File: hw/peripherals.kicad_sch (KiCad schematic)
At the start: 22 parts, among them Q2 N-Channel, SW1 SW_DPST, U10 MB85RC256VPNF-G-JNERE1, U11 DS3231M, U9 PCA9536D

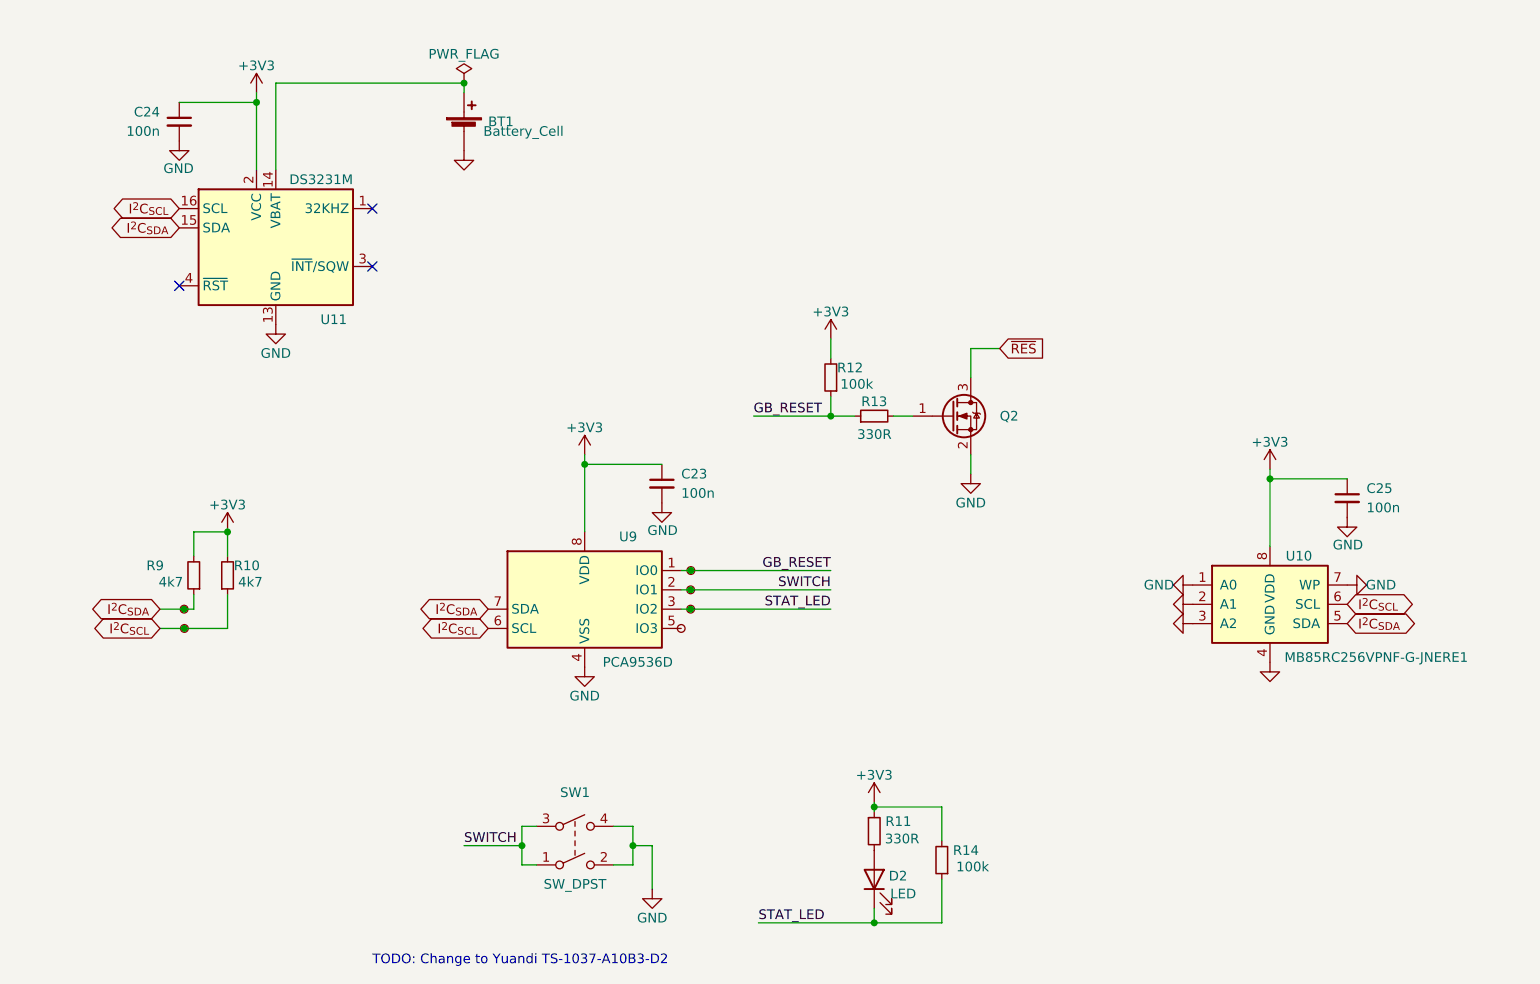
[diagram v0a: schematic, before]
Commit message: hw: multiplex Game Boy bus pins
Signed-off-by: Mahyar Koshkouei <mk@deltabeard.com>
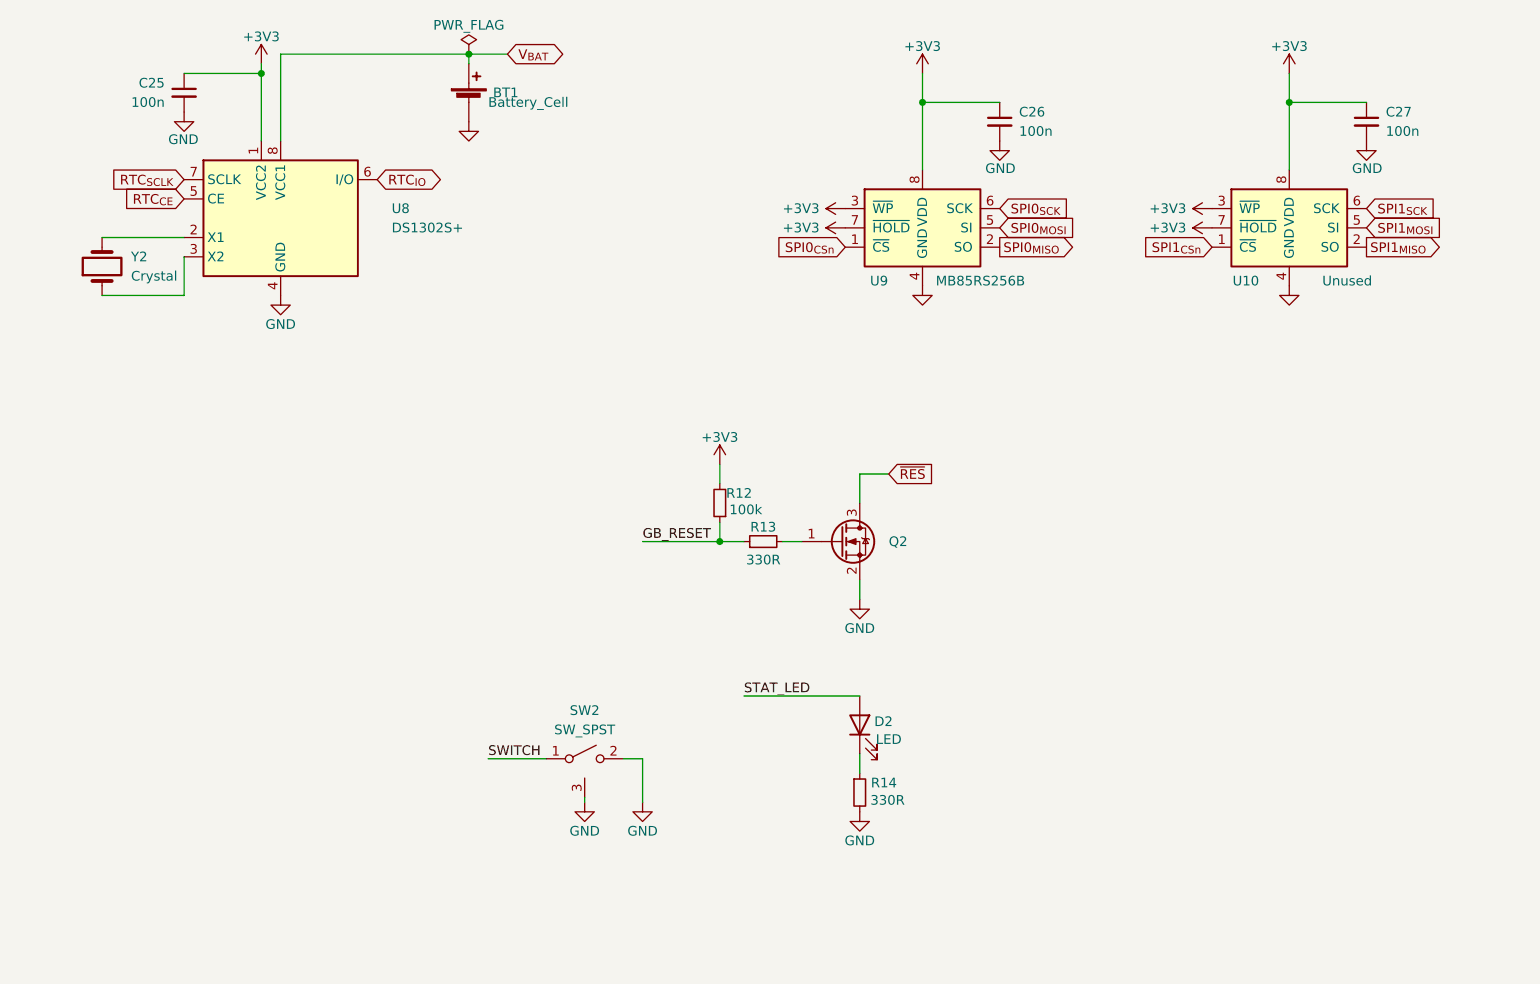
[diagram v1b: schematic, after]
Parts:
- removed C23: 100n, Capacitor_SMD:C_0402_1005Metric, symbol Device:C_Small
- removed R10, R9: 4k7, Resistor_SMD:R_0402_1005Metric, symbol Device:R_Small
- removed R14: 100k, Resistor_SMD:R_0603_1608Metric, symbol Device:R_Small
- removed SW1: SW_DPST, Project_Specific:K2-1114SA-A4SW-06, symbol Switch:SW_DPST
- removed TP40, TP41, TP42, TP43, TP44, TP45: TestPoint_Small, TestPoint:TestPoint_Pad_D1.0mm, symbol Connector:TestPoint_Small
- removed U10: MB85RC256VPNF-G-JNERE1, Package_SO:SOIC-8_3.9x4.9mm_P1.27mm, symbol Project_specific:MB85RC256V
- removed U11: DS3231M, Package_SO:SOIC-16W_7.5x10.3mm_P1.27mm, symbol Timer_RTC:DS3231M
- removed U9: PCA9536D, Package_SO:SOIC-8_3.9x4.9mm_P1.27mm, symbol Interface_Expansion:PCA9536D
- added C27: 100n, Capacitor_SMD:C_0402_1005Metric, symbol Device:C_Small
- added SW2: SW_SPST, symbol Switch:SW_SPST
- added U10: Unused, symbol Memory_NVRAM:MB85RS256B
- added U8: DS1302S+, Package_SO:SO-8_5.3x6.2mm_P1.27mm, symbol Timer_RTC:DS1302S+
- added U9: MB85RS256B, symbol Memory_NVRAM:MB85RS256B
- added Y2: Crystal, symbol Device:Crystal
- renumbered C24 to C25, C25 to C26, R11 to R14
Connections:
- net +3V3: now also C27.1, U10.3 (~{WP}), U10.7 (~{HOLD}), U10.8 (VDD), U8.1 (VCC2), U9.3 (~{WP}), U9.7 (~{HOLD}), U9.8 (VDD); no longer R14.1
- net GND: now also R14.2, C27.2, SW2.2 (B), SW2.3 (Shell), U10.4 (GND), U8.4 (GND), U9.4 (GND)
- net STAT_LED: now also D2.2 (A); no longer D2.1 (K)
- net SWITCH: now also SW2.1 (A)
- net V_{BAT}: now reaches BT1.1 (+)
- net V_{BAT}: now also U8.8 (VCC1)
- new net: D2.1 (K), R14.1
- new net: U8.2 (X1), Y2.2
- new net: U8.3 (X2), Y2.1
- new net RTC_{CE}: U8.5 (CE)
- new net RTC_{IO}: U8.6 (I/O)
- new net RTC_{SCLK}: U8.7 (SCLK)
- new net SPI0_{CSn}: U9.1 (~{CS})
- new net SPI0_{MISO}: U9.2 (SO)
- new net SPI0_{MOSI}: U9.5 (SI)
- new net SPI0_{SCK}: U9.6 (SCK)
- new net SPI1_{CSn}: U10.1 (~{CS})
- new net SPI1_{MISO}: U10.2 (SO)
- new net SPI1_{MOSI}: U10.5 (SI)
- new net SPI1_{SCK}: U10.6 (SCK)
- no-connect marks 3 -> 0
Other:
- note removed: "TODO: Change to Yuandi TS-1037-A10B3-D2"
- moved on the sheet: BT1, C25, C26, D2, Q2, R12, R13, R14

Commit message: hw: begin layout
Signed-off-by: Mahyar Koshkouei <mk@deltabeard.com>
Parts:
- removed C27: 100n, Capacitor_SMD:C_0402_1005Metric, symbol Device:C_Small
- removed U10: Unused, symbol Memory_NVRAM:MB85RS256B
- removed U8: DS1302S+, Package_SO:SO-8_5.3x6.2mm_P1.27mm, symbol Timer_RTC:DS1302S+
- removed Y2: Crystal, symbol Device:Crystal
- added U8: DS1307Z+, Package_SO:SO-8_3.9x4.9mm_P1.27mm, symbol Timer_RTC:DS1307Z+
- added Y2: 32.768k-12.5pF, Project_Specific:Crystal_DS26_D2.0mm_L6.0mm_Horizontal_1EP_style1, symbol Device:Crystal_Small
- SW3: renamed from SW2; footprint (none) -> Project_Specific:TS-1037-A10B3-D2; LCSC (none) -> C499330; MFr (none) -> TS-1037-A10B3-D2; Notes (none) -> Alternative manufacturer is acceptable
- U9: footprint (none) -> Package_SO:SOIC-8_3.9x4.9mm_P1.27mm; LCSC (none) -> C8742; MFr (none) -> MB85RS256BPNF-G-JNERE1; Manufacturer (none) -> Fujitsu; Notes (none) -> Alternative: FM25W256-GTR
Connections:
- net +3V3: now also U8.8 (VCC)
- net GND: now also U8.4 (GND)
- net V_{BAT}: now also U8.3 (VBAT)
- new net: U8.2 (X2), Y2.1
- new net: U8.1 (X1), Y2.2
- new net I2C_{SCLK}: U8.6 (SCL)
- new net I2C_{SDA}: U8.5 (SDA)
- no-connect marks 0 -> 1
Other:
- moved on the sheet: BT1, C25

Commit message: hw: WIP
Signed-off-by: Mahyar Koshkouei <mk@deltabeard.com>
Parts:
- removed SW3: SW_SPST, Project_Specific:TS-1037-A10B3-D2, symbol Switch:SW_SPST
- added C27: 100n, Capacitor_SMD:C_0402_1005Metric, symbol Device:C_Small
- added D3: SM4007PL, Diode_SMD:D_SOD-123F, symbol Diode:1N4448W
- added M1: Motor_DC, Connector_PinHeader_1.27mm:PinHeader_1x02_P1.27mm_Vertical, symbol Motor:Motor_DC
- added Q3: N-Channel, Package_TO_SOT_SMD:SOT-23, symbol Device:Q_NMOS_GSD
- added R14: 330R, Resistor_SMD:R_0603_1608Metric, symbol Device:R_Small
- added SW2: SW_SPST, Button_Switch_SMD:SW_SPST_TL3342, symbol Switch:SW_SPST
- Q2: Manufacturer Changjiang Electronics Tech (CJ) -> Changjiang Electronics Tech (CJ)
- R11: renamed from R12; Manufacturer UNI-ROYAL(Uniroyal Elec) -> UNI-ROYAL(Uniroyal Elec)
- R12: renamed from R13; Manufacturer UNI-ROYAL(Uniroyal Elec) -> UNI-ROYAL(Uniroyal Elec)
- R13: renamed from R14; Manufacturer UNI-ROYAL(Uniroyal Elec) -> UNI-ROYAL(Uniroyal Elec)
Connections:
- net GND: now also Q3.2 (S), SW2.2 (B)
- net SWITCH: now also SW2.1 (A)
- new net: Q3.1 (G), R14.2
- new net: C27.1, D3.2 (A), M1.2 (-), Q3.3 (D)
- new net +5V: C27.2, D3.1 (K), M1.1 (+)
- new net MOTOR: R14.1
